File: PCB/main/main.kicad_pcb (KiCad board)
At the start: 2 copper layers, 251.5 x 144.8 mm, 50 parts, among them IC1 LM358DR2G, IC2 ap2007, IC3 TP4056-42-ESOP8, IC4 LM3940IMP-3.3_NOPB, IC5 CP2102-GMR, J1 Conn_01x33_Female, J2 Conn_01x33_Female, J3 Conn_01x33_Female, J4 Conn_01x33_Female, Q1 AO3401A, U1 LM61BIZ/NOPD_TempSensor(TO-92), U2 LPS22HBTR_Barometer, U3 CAT24C256, U4 MICROXNJ

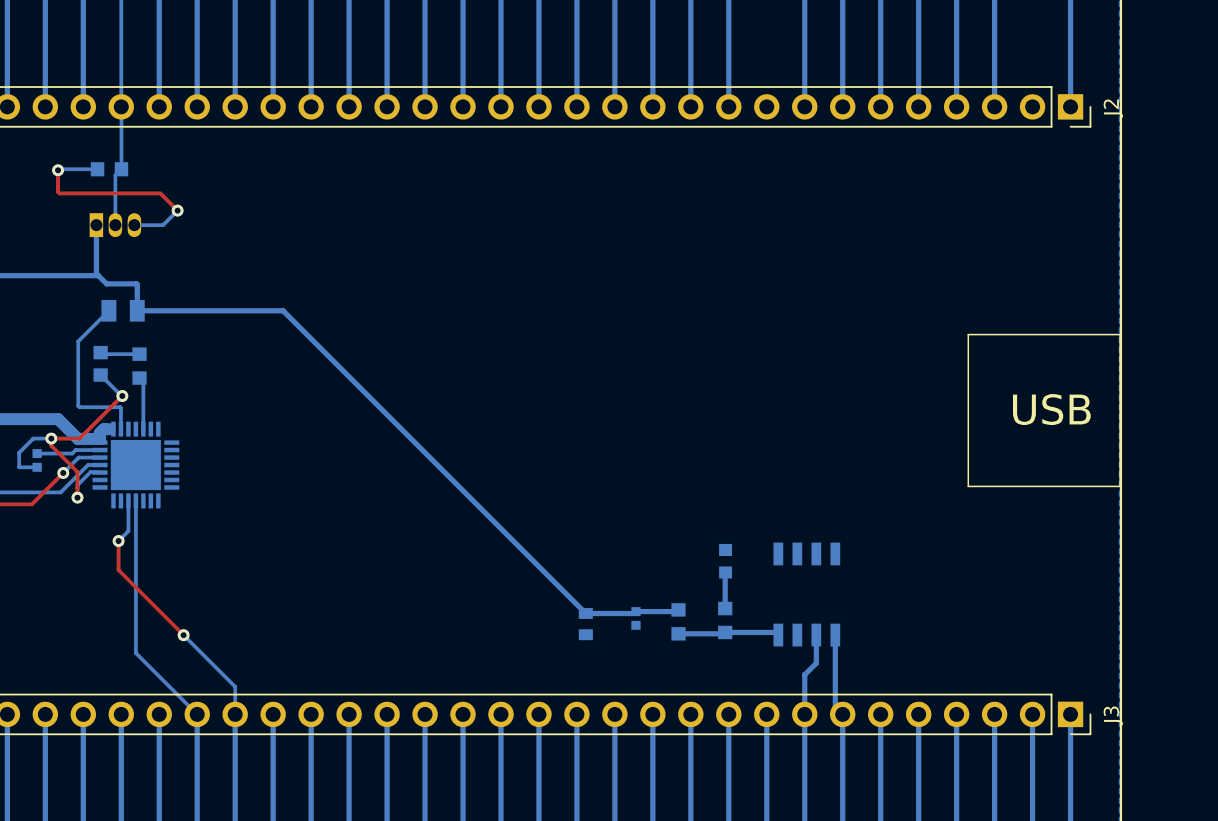
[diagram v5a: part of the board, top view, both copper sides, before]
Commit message: Ran ERC and DRV
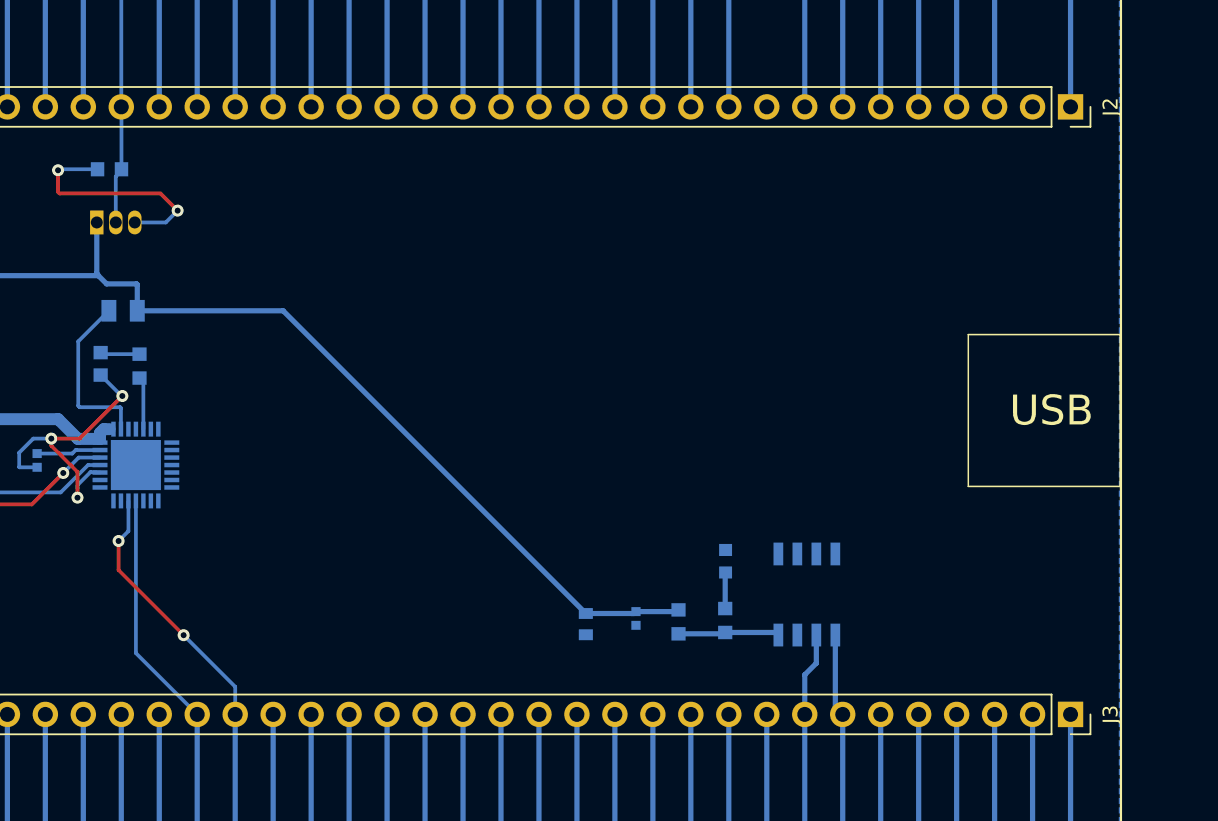
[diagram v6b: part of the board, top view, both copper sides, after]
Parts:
- moved U1 0.18 mm to (121.4, 83.3)
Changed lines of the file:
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@@
     (property "Sheetname" "")
     (attr through_hole)
-    (fp_text reference "J2" (at 0 -2.77 90) (layer "F.SilkS")
+    (fp_text reference "J2" (at 0 -2.68 90) (layer "F.SilkS")
       (effects (font (size 1 1) (thickness 0.15)))
     )
@@
     (property "Sheetname" "")
     (attr through_hole)
-    (fp_text reference "J3" (at 0 -2.77 90) (layer "F.SilkS")
+    (fp_text reference "J3" (at 0 -2.68 90) (layer "F.SilkS")
       (effects (font (size 1 1) (thickness 0.15)))
     )
@@
   )
   (footprint "EEE3088F_Footprints:TO-92-3_L4.9-W3.7-P1.27-L" (layer "B.Cu")
-    (at 121.3866 83.519491)
+    (at 121.412 83.34169)
     (property "Sheetfile" "sensing.kicad_sch")
     (property "Sheetname" "Sensing")
@@
   (segment (start 95.53 62.7) (end 95.53 60.88) (width 0.35) (layer "B.Cu") (net 2))
   (segment (start 108.9762 79.6878) (end 110.1122 79.6878) (width 0.25) (layer "B.Cu") (net 2))
-  (segment (start 124.580509 83.519491) (end 125.55 82.55) (width 0.25) (layer "B.Cu") (net 2))
   (segment (start 92.35 64.7) (end 92.35 63.6) (width 0.35) (layer "B.Cu") (net 2))
   (segment (start 114.95 98.740978) (end 114.95 99.7) (width 0.25) (layer "B.Cu") (net 2))
   (segment (start 103.7 78.2) (end 104 77.9) (width 0.25) (layer "B.Cu") (net 2))
-  (segment (start 122.85 83.712891) (end 122.6566 83.519491) (width 0.25) (layer "B.Cu") (net 2))
   (segment (start 92.95 60.2) (end 92.95 58.94) (width 0.35) (layer "B.Cu") (net 2))
   (segment (start 107.0762 81.686822) (end 107.0762 80.6878) (width 0.25) (layer "B.Cu") (net 2))
@@
   (segment (start 110.1122 79.6878) (end 110.9 78.9) (width 0.25) (layer "B.Cu") (net 2))
   (segment (start 105.37 38.15) (end 105.37 40.98) (width 0.25) (layer "B.Cu") (net 2))
+  (segment (start 124.75831 83.34169) (end 122.682 83.34169) (width 0.25) (layer "B.Cu") (net 2))
   (segment (start 117.6186 79.7814) (end 120.193 79.7814) (width 0.25) (layer "B.Cu") (net 2))
   (segment (start 100.139 45.339) (end 101.55 46.75) (width 0.25) (layer "B.Cu") (net 2))
-  (segment (start 122.6566 83.519491) (end 124.580509 83.519491) (width 0.25) (layer "B.Cu") (net 2))
   (segment (start 107.0762 80.1878) (end 107.0762 80.6878) (width 0.25) (layer "B.Cu") (net 2))
   (segment (start 120.3582 100.068) (end 119.720385 100.042511) (width 0.25) (layer "B.Cu") (net 2))
+  (segment (start 125.55 82.55) (end 124.75831 83.34169) (width 0.25) (layer "B.Cu") (net 2))
   (segment (start 100 96.25) (end 99.8082 96.0582) (width 0.35) (layer "B.Cu") (net 2))
   (segment (start 107.939378 82.55) (end 107.0762 81.686822) (width 0.25) (layer "B.Cu") (net 2))
@@
   (segment (start 126.86 65.45) (end 126.86 75.61) (width 0.35) (layer "B.Cu") (net 23))
   (segment (start 124.32 65.45) (end 124.32 75.61) (width 0.35) (layer "B.Cu") (net 24))
+  (segment (start 121.793 79.7814) (end 121.793 79.883) (width 0.25) (layer "B.Cu") (net 25))
   (segment (start 121.793 79.7814) (end 121.793 75.623) (width 0.25) (layer "B.Cu") (net 25))
-  (segment (start 121.3866 80.1878) (end 121.793 79.7814) (width 0.25) (layer "B.Cu") (net 25))
+  (segment (start 121.793 79.883) (end 121.412 80.264) (width 0.25) (layer "B.Cu") (net 25))
+  (segment (start 121.412 80.264) (end 121.412 83.34169) (width 0.25) (layer "B.Cu") (net 25))
   (segment (start 121.793 75.623) (end 121.78 75.61) (width 0.25) (layer "B.Cu") (net 25))
   (segment (start 121.78 75.61) (end 121.78 65.45) (width 0.25) (layer "B.Cu") (net 25))
-  (segment (start 121.3866 83.519491) (end 121.3866 80.1878) (width 0.25) (layer "B.Cu") (net 25))
   (segment (start 119.24 65.45) (end 119.24 75.61) (width 0.35) (layer "B.Cu") (net 26))
   (segment (start 116.7 75.61) (end 116.7 65.45) (width 0.35) (layer "B.Cu") (net 27))
@@
   (via (at 103.05 61.05) (size 0.8) (drill 0.4) (layers "F.Cu" "B.Cu") (net 68))
   (segment (start 120.8 87.45) (end 122.8 87.45) (width 0.35) (layer "B.Cu") (net 68))
+  (segment (start 120.1166 86.7666) (end 120.142 86.7412) (width 0.35) (layer "B.Cu") (net 68))
   (segment (start 94.1824 47.921078) (end 94.1824 48.7794) (width 0.6) (layer "B.Cu") (net 68))
   (segment (start 94.1824 48.7794) (end 101.39 55.987) (width 0.6) (layer "B.Cu") (net 68))
@@
   (segment (start 103.0384 61.0616) (end 103.05 61.05) (width 0.35) (layer "B.Cu") (net 68))
   (segment (start 103.186711 80.932036) (end 109.154675 86.9) (width 0.35) (layer "B.Cu") (net 68))
-  (segment (start 120.1166 84.0166) (end 120.1166 83.519491) (width 0.25) (layer "B.Cu") (net 68))
   (segment (start 156.083 109.4994) (end 156.21 109.3724) (width 0.35) (layer "B.Cu") (net 68))
   (segment (start 122.8 87.45) (end 122.85 87.5) (width 0.35) (layer "B.Cu") (net 68))
-  (segment (start 120.1166 86.7666) (end 120.1166 83.519491) (width 0.35) (layer "B.Cu") (net 68))
   (segment (start 158.9406 109.3724) (end 159.0548 109.2582) (width 0.35) (layer "B.Cu") (net 68))
   (segment (start 109.154675 86.9) (end 120.25 86.9) (width 0.35) (layer "B.Cu") (net 68))
@@
   (segment (start 132.6078 89.25) (end 152.8572 109.4994) (width 0.35) (layer "B.Cu") (net 68))
   (segment (start 102.813289 79.663289) (end 103.186711 79.663289) (width 0.35) (layer "B.Cu") (net 68))
+  (segment (start 120.142 86.7412) (end 120.142 83.34169) (width 0.35) (layer "B.Cu") (net 68))
   (segment (start 101.39 61.0616) (end 101.39 56.9468) (width 0.35) (layer "B.Cu") (net 68))
   (segment (start 101.39 61.0616) (end 103.0384 61.0616) (width 0.35) (layer "B.Cu") (net 68))

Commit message: Finalised and generated Gerbers.
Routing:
- net GND: track 110.3 -> 124.4 mm, vias 15 -> 16
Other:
- board size 251.5 x 144.8 mm -> 98.7 x 98.7 mm
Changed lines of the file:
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@@
       (outputformat 1)
       (mirror false)
-      (drillshape 1)
+      (drillshape 0)
       (scaleselection 1)
-      (outputdirectory "")
+      (outputdirectory "../Gerbers/")
     )
   )
@@
     )
   )
-  (gr_rect (start 90.2758 132.1363) (end 188.65 33.8637) (layer "B.SilkS") (width 0.15) (fill none))
-  (gr_rect (start 90.2758 33.7637) (end 188.65 132.0363) (layer "F.SilkS") (width 0.15) (fill none))
+  (gr_rect (start 90.2758 132.1363) (end 188.65 33.75) (layer "B.SilkS") (width 0.15) (fill none))
+  (gr_rect (start 90.2758 33.7637) (end 188.65 132.15) (layer "F.SilkS") (width 0.15) (fill none))
   (gr_rect (start 178.44 90.84) (end 188.6 101) (layer "F.SilkS") (width 0.1) (fill none))
-  (gr_rect (start 40.64 29.21) (end 292.1 173.99) (layer "Edge.Cuts") (width 0.1) (fill none))
+  (gr_rect (start 90.1 33.6) (end 188.8 132.3) (layer "Edge.Cuts") (width 0.1) (fill none))
   (gr_line (start 188.65 56.28) (end 188.65 109.62) (layer "F.Fab") (width 0.1))
   (gr_line (start 100.19 122.6) (end 100.19 69.26) (layer "F.Fab") (width 0.1))
@@
   (segment (start 117.55 81.3) (end 117.55 79.85) (width 0.25) (layer "F.Cu") (net 2))
   (segment (start 109.574614 82.55) (end 108.45 82.55) (width 0.25) (layer "F.Cu") (net 2))
+  (segment (start 101.55 46.75) (end 92.65 46.75) (width 0.25) (layer "F.Cu") (net 2))
   (segment (start 95.5 60.85) (end 93.6 60.85) (width 0.35) (layer "F.Cu") (net 2))
   (segment (start 101.55 46.75) (end 99.3 44.5) (width 0.25) (layer "F.Cu") (net 2))
@@
   (segment (start 98.15 63.35) (end 95.65 60.85) (width 0.35) (layer "F.Cu") (net 2))
   (segment (start 111.624511 79.624511) (end 111.624511 80.500103) (width 0.25) (layer "F.Cu") (net 2))
+  (segment (start 92.65 46.75) (end 92.55 46.65) (width 0.25) (layer "F.Cu") (net 2))
   (segment (start 104.2 80.85) (end 103.7 80.35) (width 0.25) (layer "F.Cu") (net 2))
   (via (at 92.95 60.2) (size 0.8) (drill 0.4) (layers "F.Cu" "B.Cu") (net 2))
@@
   (via (at 121.85 94.95) (size 0.8) (drill 0.4) (layers "F.Cu" "B.Cu") (net 2))
   (via (at 104.2 80.85) (size 0.8) (drill 0.4) (layers "F.Cu" "B.Cu") (net 2))
+  (via (at 92.55 46.65) (size 0.8) (drill 0.4) (layers "F.Cu" "B.Cu") (net 2))
   (via (at 98.15 63.35) (size 0.8) (drill 0.4) (layers "F.Cu" "B.Cu") (net 2))
   (via (at 108.45 82.55) (size 0.8) (drill 0.4) (layers "F.Cu" "B.Cu") (net 2))
@@
   (segment (start 118.85 100.912896) (end 118.85 101.1) (width 0.25) (layer "B.Cu") (net 2))
   (segment (start 95.53 60.88) (end 95.5 60.85) (width 0.35) (layer "B.Cu") (net 2))
+  (segment (start 92.55 46.65) (end 92.55 49.447) (width 0.25) (layer "B.Cu") (net 2))
   (segment (start 99.3 39.356) (end 97.4344 37.4904) (width 0.25) (layer "B.Cu") (net 2))
   (segment (start 104.4 41.95) (end 101.011 45.339) (width 0.25) (layer "B.Cu") (net 2))
@@
   (segment (start 98.61 62.89) (end 98.15 63.35) (width 0.35) (layer "B.Cu") (net 2))
   (segment (start 104 77.9) (end 104 75.61) (width 0.25) (layer "B.Cu") (net 2))
+  (segment (start 92.55 49.447) (end 94.1824 51.0794) (width 0.25) (layer "B.Cu") (net 2))
   (segment (start 114.95 99.7) (end 114.97 99.72) (width 0.25) (layer "B.Cu") (net 2))
   (segment (start 119.720385 100.042511) (end 118.85 100.912896) (width 0.25) (layer "B.Cu") (net 2))

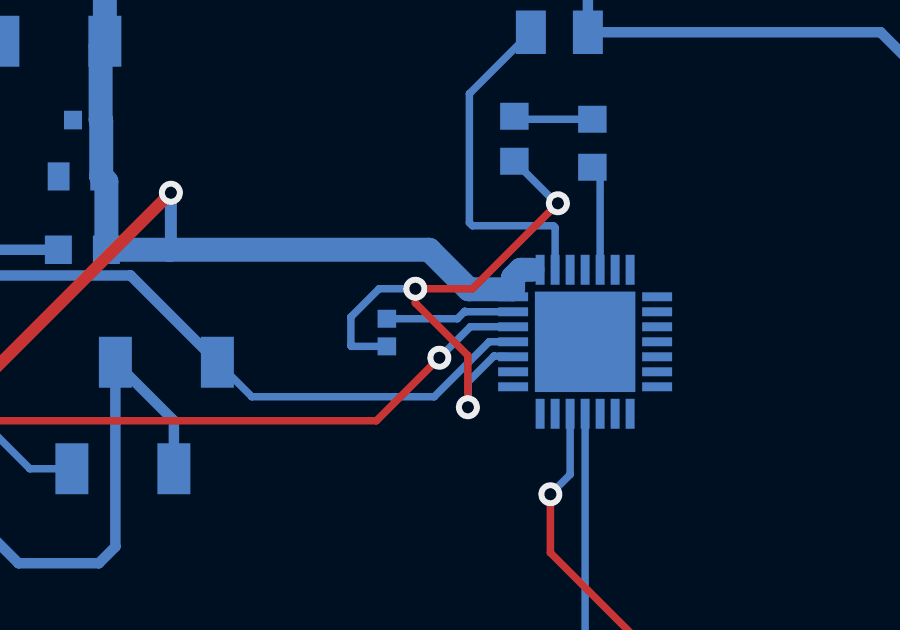
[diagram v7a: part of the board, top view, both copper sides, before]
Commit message: Added the contributors, the project name and revised the gradescope comments.
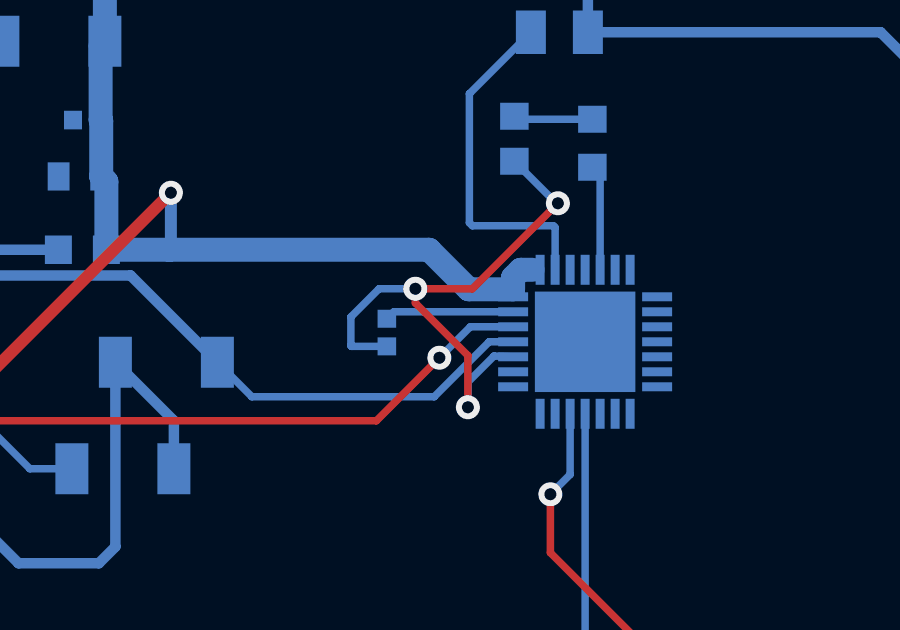
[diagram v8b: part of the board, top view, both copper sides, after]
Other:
- board text added: "Group Number 9 Caide Spriestersbach Cameron Wilson David Young"
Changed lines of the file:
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@@
       (effects (font (size 1.27 1.27) (thickness 0.254)) (justify mirror))
     )
-    (fp_text user "${REFERENCE}" (at 0 0) (layer "B.Fab")
+    (fp_text user "${REFERENCE}" (at 1 -2.1742) (layer "B.Fab")
       (effects (font (size 1.27 1.27) (thickness 0.254)) (justify mirror))
     )
@@
   (gr_line (start 188.65 122.6) (end 100.19 122.6) (layer "F.Fab") (width 0.1))
   (gr_rect (start 178.44 90.84) (end 188.6 101) (layer "F.Fab") (width 0.1) (fill none))
+  (gr_text "Group Number 9\nCaide Spriestersbach\nCameron Wilson\nDavid Young" (at 95.4 119.35 90) (layer "B.SilkS")
+    (effects (font (size 1.5 1.5) (thickness 0.3)) (justify mirror))
+  )
   (gr_text "USB" (at 184.01 95.93) (layer "F.SilkS")
     (effects (font (size 2 2) (thickness 0.3)))
@@
   (segment (start 120.25 86.9) (end 120.1166 86.7666) (width 0.35) (layer "B.Cu") (net 68))
   (segment (start 122.85 89.25) (end 132.6078 89.25) (width 0.35) (layer "B.Cu") (net 68))
-  (segment (start 118.75 98.55) (end 118.768 98.568) (width 0.25) (layer "B.Cu") (net 69))
-  (segment (start 116.15 98.8) (end 118.5 98.8) (width 0.25) (layer "B.Cu") (net 69))
-  (segment (start 118.768 98.568) (end 120.3582 98.568) (width 0.25) (layer "B.Cu") (net 69))
-  (segment (start 118.5 98.8) (end 118.75 98.55) (width 0.25) (layer "B.Cu") (net 69))
+  (segment (start 120.3582 98.568) (end 116.382 98.568) (width 0.25) (layer "B.Cu") (net 69))
+  (segment (start 116.382 98.568) (end 116.15 98.8) (width 0.25) (layer "B.Cu") (net 69))
   (segment (start 116.85 45.45) (end 116.898 45.498) (width 0.35) (layer "B.Cu") (net 70))
   (segment (start 116.898 45.498) (end 116.898 60.2488) (width 0.35) (layer "B.Cu") (net 70))
